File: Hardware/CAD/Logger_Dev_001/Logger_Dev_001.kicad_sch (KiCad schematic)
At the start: 13 parts, among them U2 ESP32-C6-WROOM-1

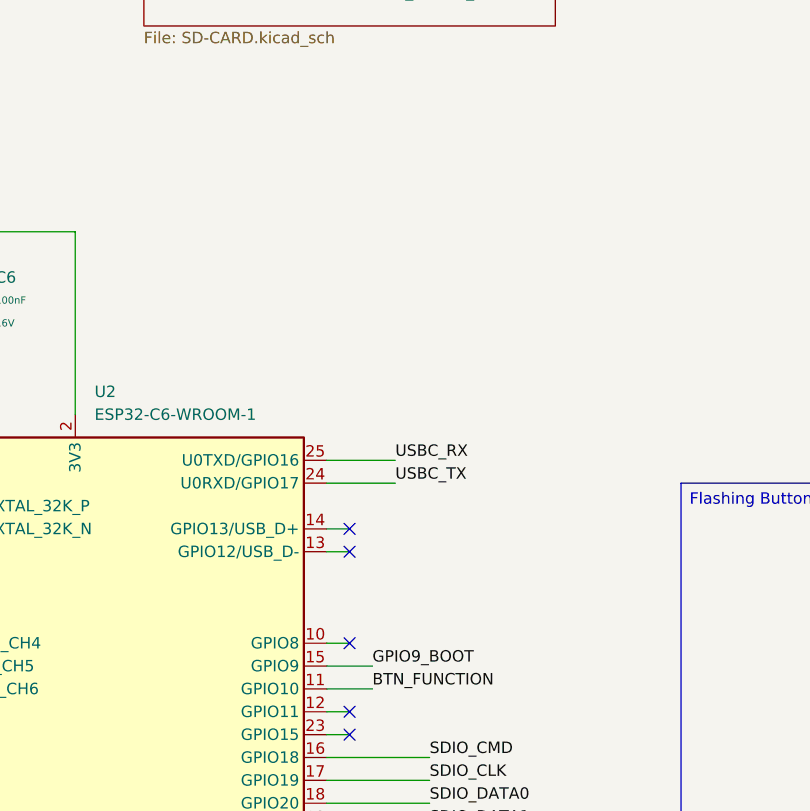
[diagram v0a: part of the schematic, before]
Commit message: Updated PCB to include strapping pin and USB C DP reroute
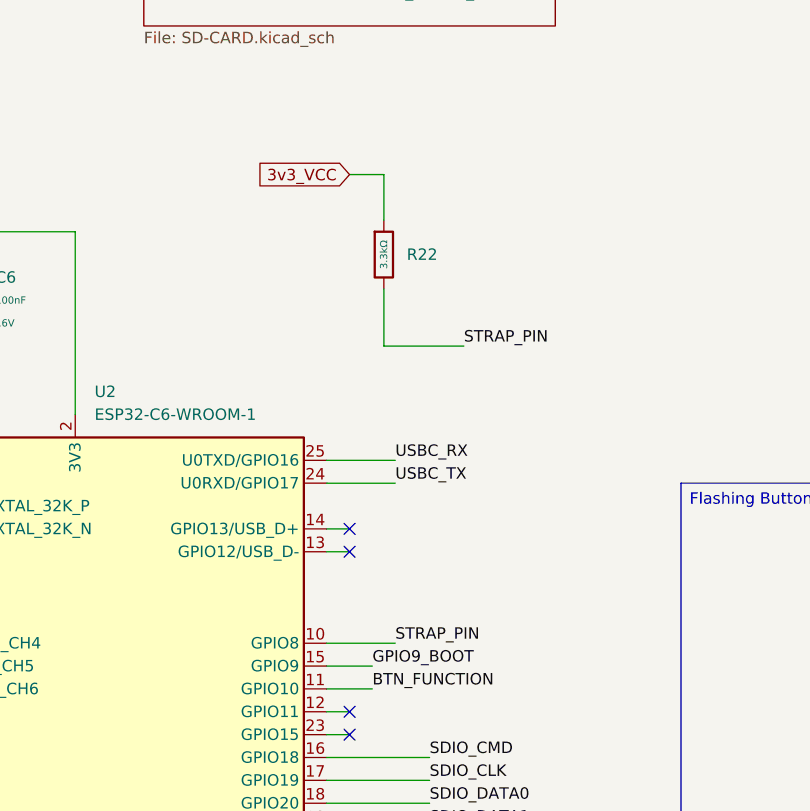
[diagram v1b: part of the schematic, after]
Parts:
- added R22: 3.3kΩ, PCM_JLCPCB:R_0402, symbol PCM_JLCPCB-Resistors:0402,3.3kΩ
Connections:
- net 3v3_VCC: now also R22.1
- net STRAP_PIN: now reaches U2.10 (GPIO8)
- net STRAP_PIN: now also R22.2
- no-connect marks 11 -> 10
